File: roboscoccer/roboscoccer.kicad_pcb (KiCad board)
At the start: 2 copper layers, 71.3 x 98 mm, 17 parts, among them J1 HC-05, J2 motordriver 1 2, J3 solar conn, J6 motordriver 3 4, U1 Buck

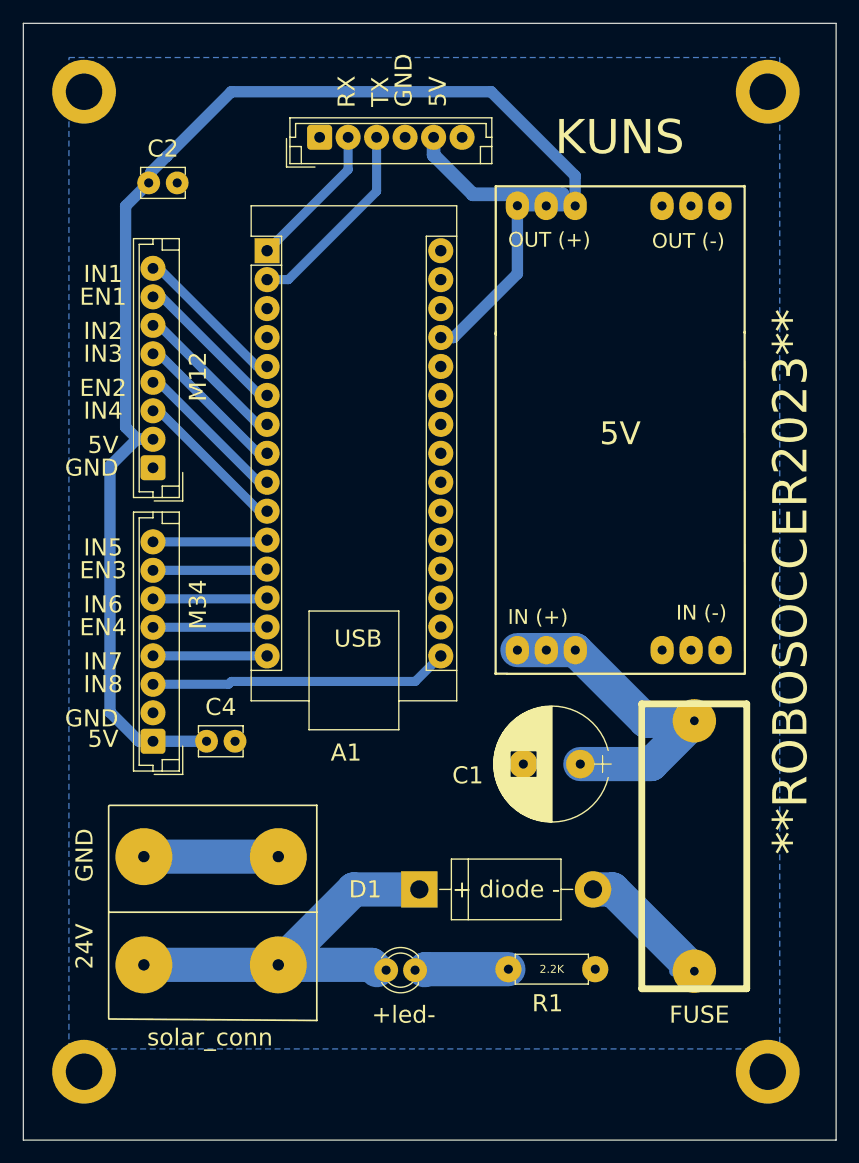
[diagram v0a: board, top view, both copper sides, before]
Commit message: Decoupling capacitors placement near 5V power output
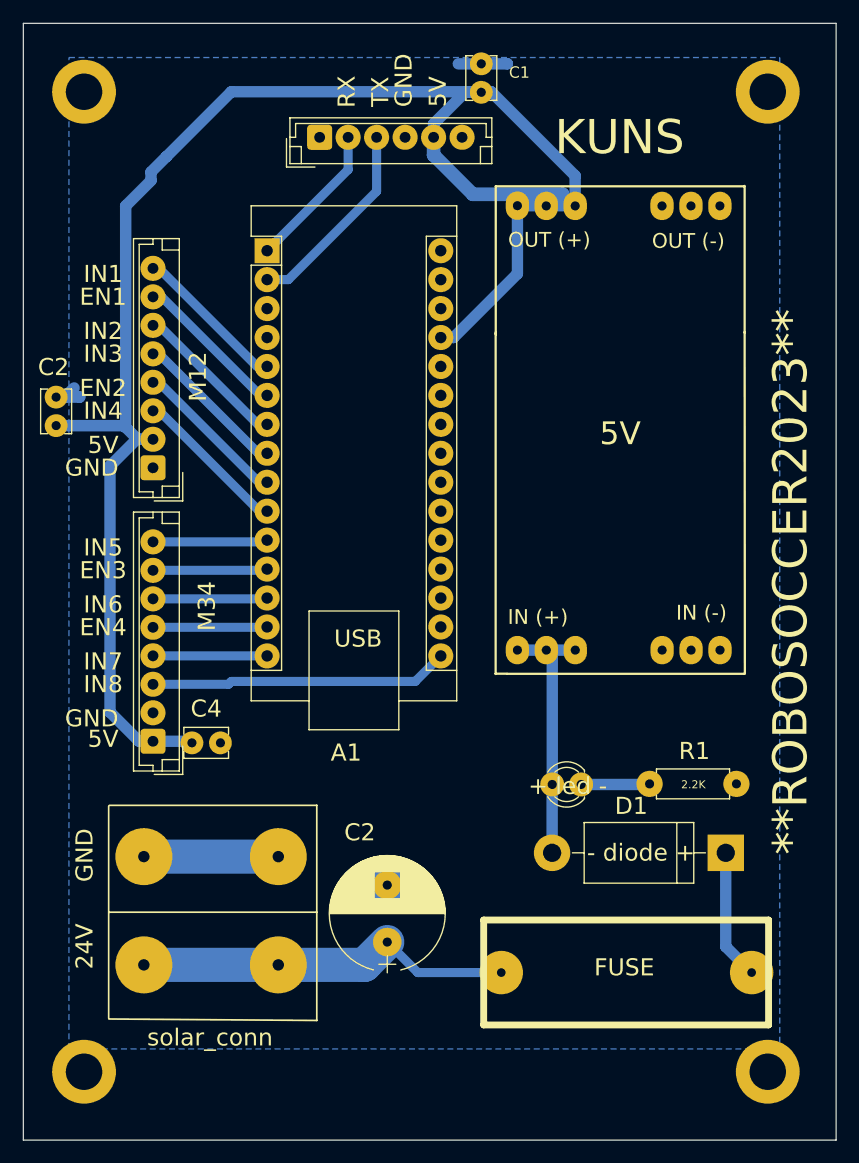
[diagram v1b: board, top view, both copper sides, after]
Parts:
- added C1: 104pF, MY_LIB:Capacitor_Disc_Small, F.Cu at (102.2, 71.0)
- A1: value Arduino_Nano_Every -> Arduino_Nano
- C2, C4: value CAP -> 104pF
- moved D2 27.1 mm to (123.6, 137.8), turned to 180 degrees
- moved C3 23.0 mm to (93.9, 145.6), turned to 90 degrees
- moved C2 22.8 mm to (64.9, 100.3), turned to 90 degrees
- moved D1 21.9 mm to (111.0, 131.8)
- moved R1 20.4 mm to (117.0, 131.7)
- moved F1 12.0 mm to (115.1, 147.8), turned to 180 degrees
- moved C4 1.29 mm to (76.8, 128.1)
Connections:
- net Net-(D1-Pad1) renamed /PWR_LED_K
- C3 pad 1: /VIN -> /24V
- D1 pad 2: /24V -> /VIN
- D2 pad 1: /24V -> /Polarity diode A
- D2 pad 2: Net-(D2-Pad2) -> /VIN
- F1 pad 1: Net-(D2-Pad2) -> /24V
- F1 pad 2: /VIN -> /Polarity diode A
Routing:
- net GND: track 11.8 -> 29.4 mm
- net Net-(D2-Pad2): track 13.6 -> 0.00 mm
- net /5V: track 144.1 -> 155.6 mm
- net /Polarity diode A: track 0.00 -> 11.4 mm
- net /VIN: track 29.7 -> 23.1 mm
- net /24V: track 35.8 -> 33.3 mm
- net /PWR_LED_K: track 7.54 -> 6.03 mm
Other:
- board text added: "+ led -"
- board text added: "- diode +"
- board text added: "C2"
- board text removed: "+ diode -"
- board text removed: "+led-"
- board text removed: "C1"
